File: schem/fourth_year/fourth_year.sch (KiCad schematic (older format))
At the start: 103 parts, among them P1 F Type, P10 BNC, P2 SAW, P3 CONNECTOR, P4 DC JACK, P5 CONNECTOR, P6 CONN_6, P7 CONN_1, P8 CONN_1, P9 CONN_6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

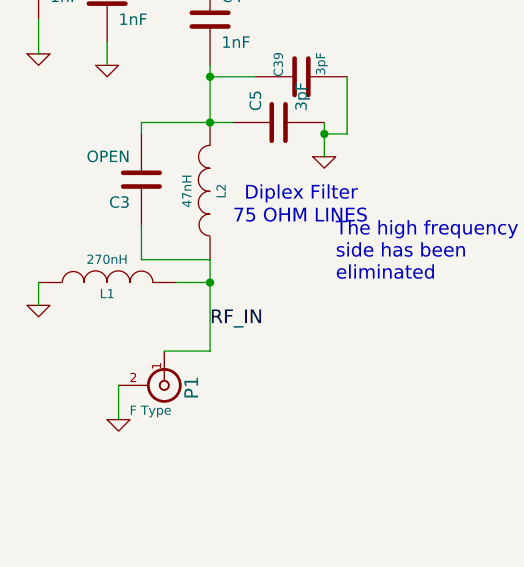
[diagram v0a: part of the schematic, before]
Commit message: Eliminated UHF input
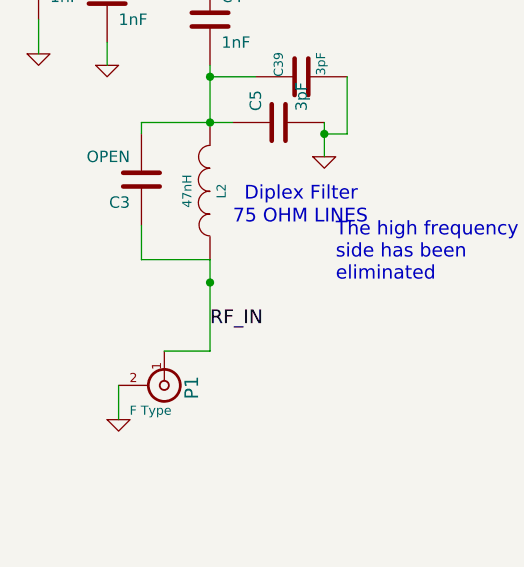
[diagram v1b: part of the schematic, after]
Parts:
- removed L1: 270nH, 1.60mm x 0.80mm, symbol INDUCTOR
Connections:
- wire segments 426 -> 424
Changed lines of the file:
@@
-$EndComp
-$Comp
-L GND #PWR052
-U 1 1 542CB667
-P 800 7250
-F 0 "#PWR052" H 800 7250 30  0001 C CNN
-F 1 "GND" H 800 7180 30  0001 C CNN
-F 2 "" H 800 7250 60  0001 C CNN
-F 3 "" H 800 7250 60  0001 C CNN
-	1    800  7250
-	1    0    0    -1
-$EndComp
-$Comp
-L INDUCTOR L1
-U 1 1 542CB61E
-P 1100 7150
-F 0 "L1" V 1050 7150 40  0000 C CNN
-F 1 "270nH" V 1200 7150 40  0000 C CNN
-F 2 "1.60mm x 0.80mm" H 1100 7150 60  0001 C CNN
-F 3 "" H 1100 7150 60  0001 C CNN
-	1    1100 7150
-	0    -1   -1   0
 $EndComp
 $Comp
@@
 	1550 6450 1550 6200
 Wire Wire Line
-	800  7250 800  7150
-Wire Wire Line
 	1150 7750 1150 7600
 Wire Wire Line
@@
 Text Label 1550 7350 0    60   ~ 0
 RF_IN
-Wire Wire Line
-	1400 7150 1550 7150
 Text Notes 2100 7150 0    60   ~ 0
 The high frequency\nside has been\neliminated

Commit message: Progress on main PCB
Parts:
- added C10, C53: 3uF, ~, symbol C
- added C6: 10uF, ~, symbol C
- added C8: .1uF, ~, symbol C
- added P11, P12: CONNECTOR, FEMALE CONN THROUGH HOLE, symbol CONNECTOR
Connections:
- wire segments 424 -> 440
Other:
- note added: "POWER STAR ROOT\nFOR MAX3543"
- moved on the sheet: C17

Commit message: Router power
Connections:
- wire segments 440 -> 441
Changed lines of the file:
@@
 F 3 "" H 16650 1550 60  0001 C CNN
 	1    16650 1550
-	1    0    0    -1
+	1    0    0    1
 $EndComp
 $Comp
@@
 	8100 5600 8100 5450
 Connection ~ 8100 5450
-Wire Wire Line
-	16650 1750 16650 1800
-Wire Wire Line
-	16650 1800 16900 1800
 Connection ~ 16900 1800
 Wire Wire Line
@@
 Wire Wire Line
 	2900 8500 2900 8650
+Wire Wire Line
+	16650 1750 16650 1800
+Wire Wire Line
+	16650 1800 16900 1800
+Wire Wire Line
+	16550 1350 16650 1350
+Connection ~ 16650 1350
 $EndSCHEMATC
